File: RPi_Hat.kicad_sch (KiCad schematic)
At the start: 38 parts, among them IC1 0.96_I2C_OLED, IC2 0.96_I2C_OLED, J1 RPi_GPIO, J2 TCBM, J3 Conn_01x05, J4 Mini-DIN-7, J5 Conn_01x07, Q1 MMBT3904, Q2 MMBT3904, Q3 MMBT3904, Q4 MMBT3904, SW1 Select, SW2 Up, SW3 Down, SW4 Exit, SW5 Add Disk, SW6 RotaryEncoder_Switch

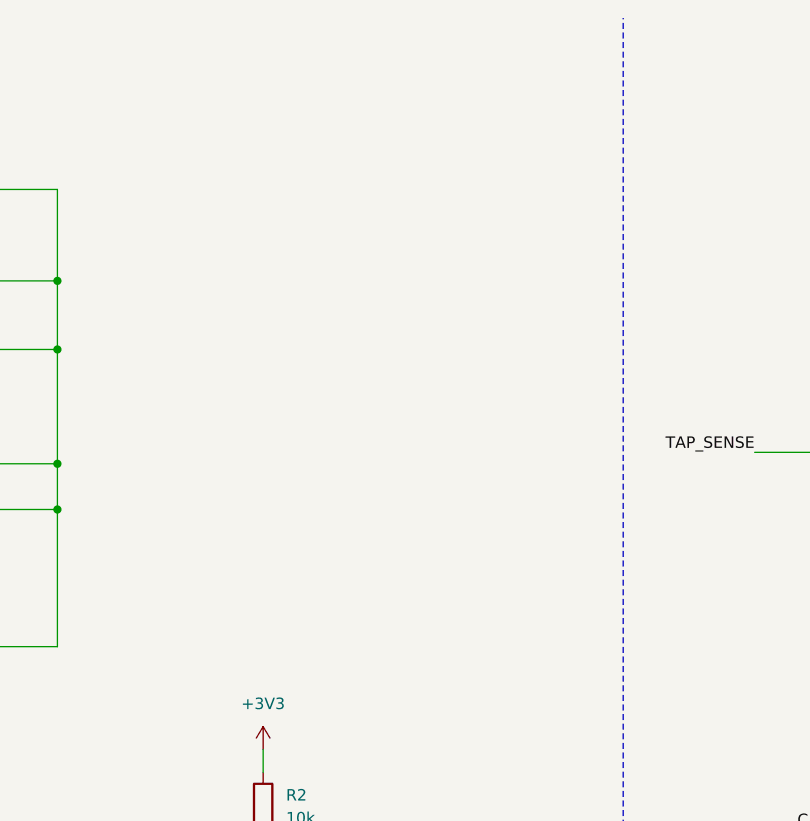
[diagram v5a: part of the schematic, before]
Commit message: TCBM pullups are required
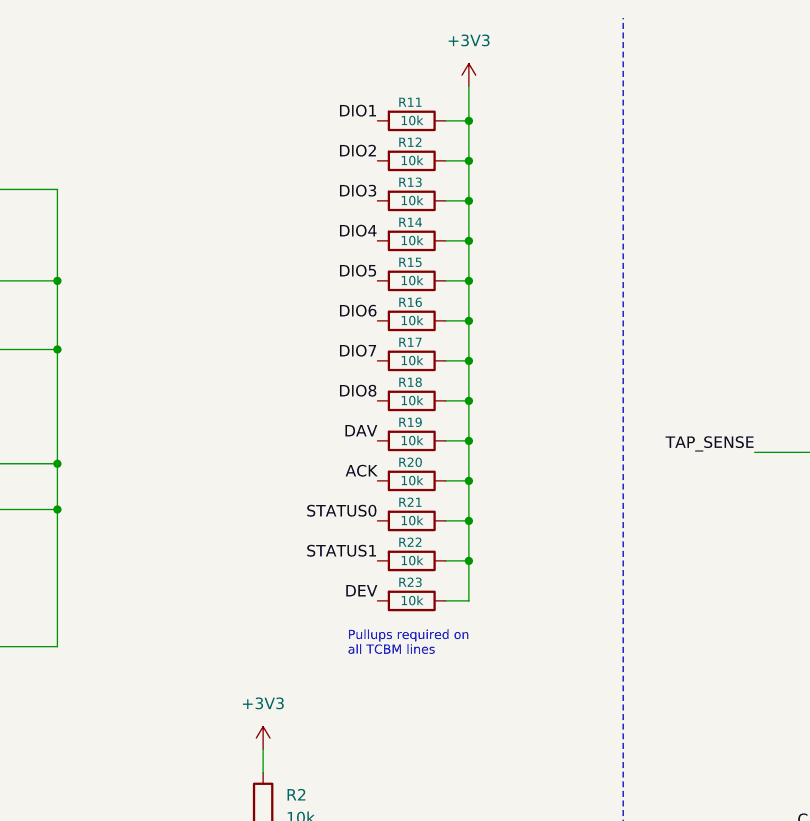
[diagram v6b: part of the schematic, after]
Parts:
- added R11, R12, R13, R14, R15, R16, R17, R18, R19, R20, R21, R22, R23: 10k, Resistor_SMD:R_0805_2012Metric_Pad1.20x1.40mm_HandSolder, symbol Device:R
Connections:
- net +3V3: now also R11.1, R12.1, R13.1, R14.1, R15.1, R16.1, R17.1, R18.1, R19.1, R20.1, R21.1, R22.1, R23.1
- net ACK: now also R20.2
- net DAV: now also R19.2
- net DEV: now also R23.2
- net DIO1: now also R11.2
- net DIO2: now also R12.2
- net DIO3: now also R13.2
- net DIO4: now also R14.2
- net DIO5: now also R15.2
- net DIO6: now also R16.2
- net DIO7: now also R17.2
- net DIO8: now also R18.2
- net STATUS0: now also R21.2
- net STATUS1: now also R22.2
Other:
- note added: "Pullups required on all TCBM lines"
